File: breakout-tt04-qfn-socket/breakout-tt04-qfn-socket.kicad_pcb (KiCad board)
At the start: 2 copper layers, 45 x 52.5 mm, 104 parts, among them U1 Caravel_QFN_Socket

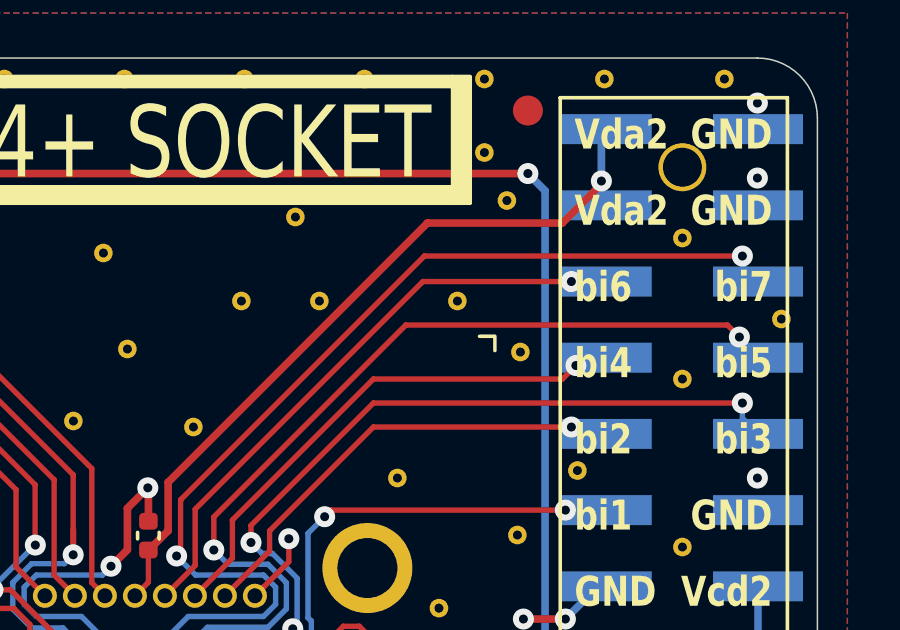
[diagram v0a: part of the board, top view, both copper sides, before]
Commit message: add PIN1 marker for QFN socket board
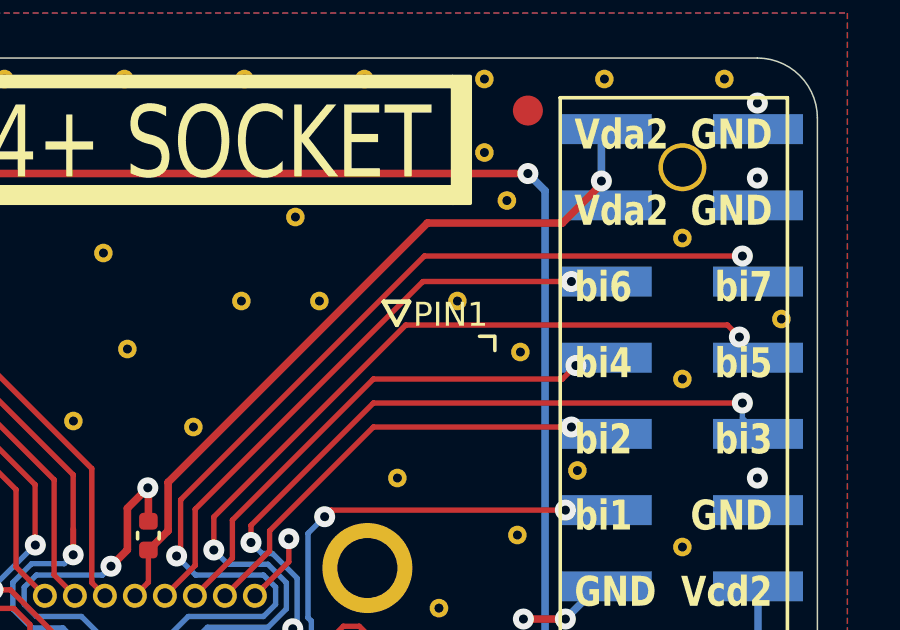
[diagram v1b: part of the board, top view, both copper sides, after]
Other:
- board text added: "PIN1"
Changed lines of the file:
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@@
 		(layer "F.SilkS")
 	)
+	(gr_poly
+		(pts
+			(xy 78.982529 26.396539) (xy 79.393472 25.621539) (xy 78.543472 25.621539)
+		)
+		(stroke
+			(width 0.15)
+			(type solid)
+		)
+		(fill none)
+		(layer "F.SilkS")
+	)
 	(gr_rect
 		(start 48.67744 18.77256)
@@
 		)
 	)
+	(gr_text "PIN1"
+		(at 79.518472 26.521539 0)
+		(layer "F.SilkS")
+		(effects
+			(font
+				(size 0.8 0.8)
+				(thickness 0.15)
+			)
+			(justify left bottom)
+		)
+	)
